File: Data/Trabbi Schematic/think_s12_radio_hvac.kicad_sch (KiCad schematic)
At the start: 20 parts, among them K1 Heated RW Relay R2, K2 Blower Relay R12, K3 Recirculation Relay R14, K4 Combustion Heater Relay R16, M1 Brake Vacuum Pump (E14), M2 Heater Blower Motor, M3 Recirculation Motor, SW1 Heater Switch, SW2 Recirculation Switch, SW3 Tailgate Release Switch, U1 Radio Unit, U2 Supplementary Heater (Webasto)

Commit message: Fix wire-to-pin connections: use exact calculated pin positions
Refactored gen_think_complete.py to compute exact pin schematic
coordinates instead of using approximate manual offsets. Added p()
method to Sheet class that transforms symbol-local pin positions to
schematic coordinates. All 232 wire calls across 13 sub-sheet
generators now use p() for pin endpoints, fixing misaligned
connections (previously off by 0.54-10+ units).

Co-Authored-By: Claude Opus 4.6 <noreply@anthropic.com>
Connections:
- net +12V_F1_HTDWS: now also K1.1 (86_COIL+)
- net +12V_F22_VACPUMP: now also M1.1 (+)
- net +12V_F33_WEBASTO: now also K4.1 (86_COIL+)
- net +12V_F3_HEATER: now also U2.1 (+12V)
- net +12V_F5_BLOWER: now also SW1.1 (IN), SW2.1 (A)
- net +12V_F7_RADIO: now also U1.1 (+12V_BAT)
- net +12V_F9_HORN_DOME: now also SW3.1 (A)
- net GND: now also HR1.2 (GND), LS1.2 (-), LS2.2 (-), M1.2 (-), M2.2 (M-), M3.2 (M-), SOL1.2 (-), U1.2 (GND), U1.5 (SPK_L-), U1.7 (SPK_R-), U2.2 (GND)
- net TAILGATE_RELEASE: now also SOL1.1 (+)
- net WEBASTO_CTRL: now also U2.5 (CTRL)
- net at HR1.1 (+12V): now also K1.3 (30_COM)
- net at M2.1 (M+): now also K2.3 (30_COM)
- net at SW2.2 (B): now also K3.1 (86_COIL+)
- net at LS1.1 (+): now also U1.4 (SPK_L+)
- net at U1.6 (SPK_R+): now also LS2.1 (+)
- net at M3.1 (M+): now also K3.3 (30_COM)
- net at K2.1 (86_COIL+): now also SW1.3 (SPD1)

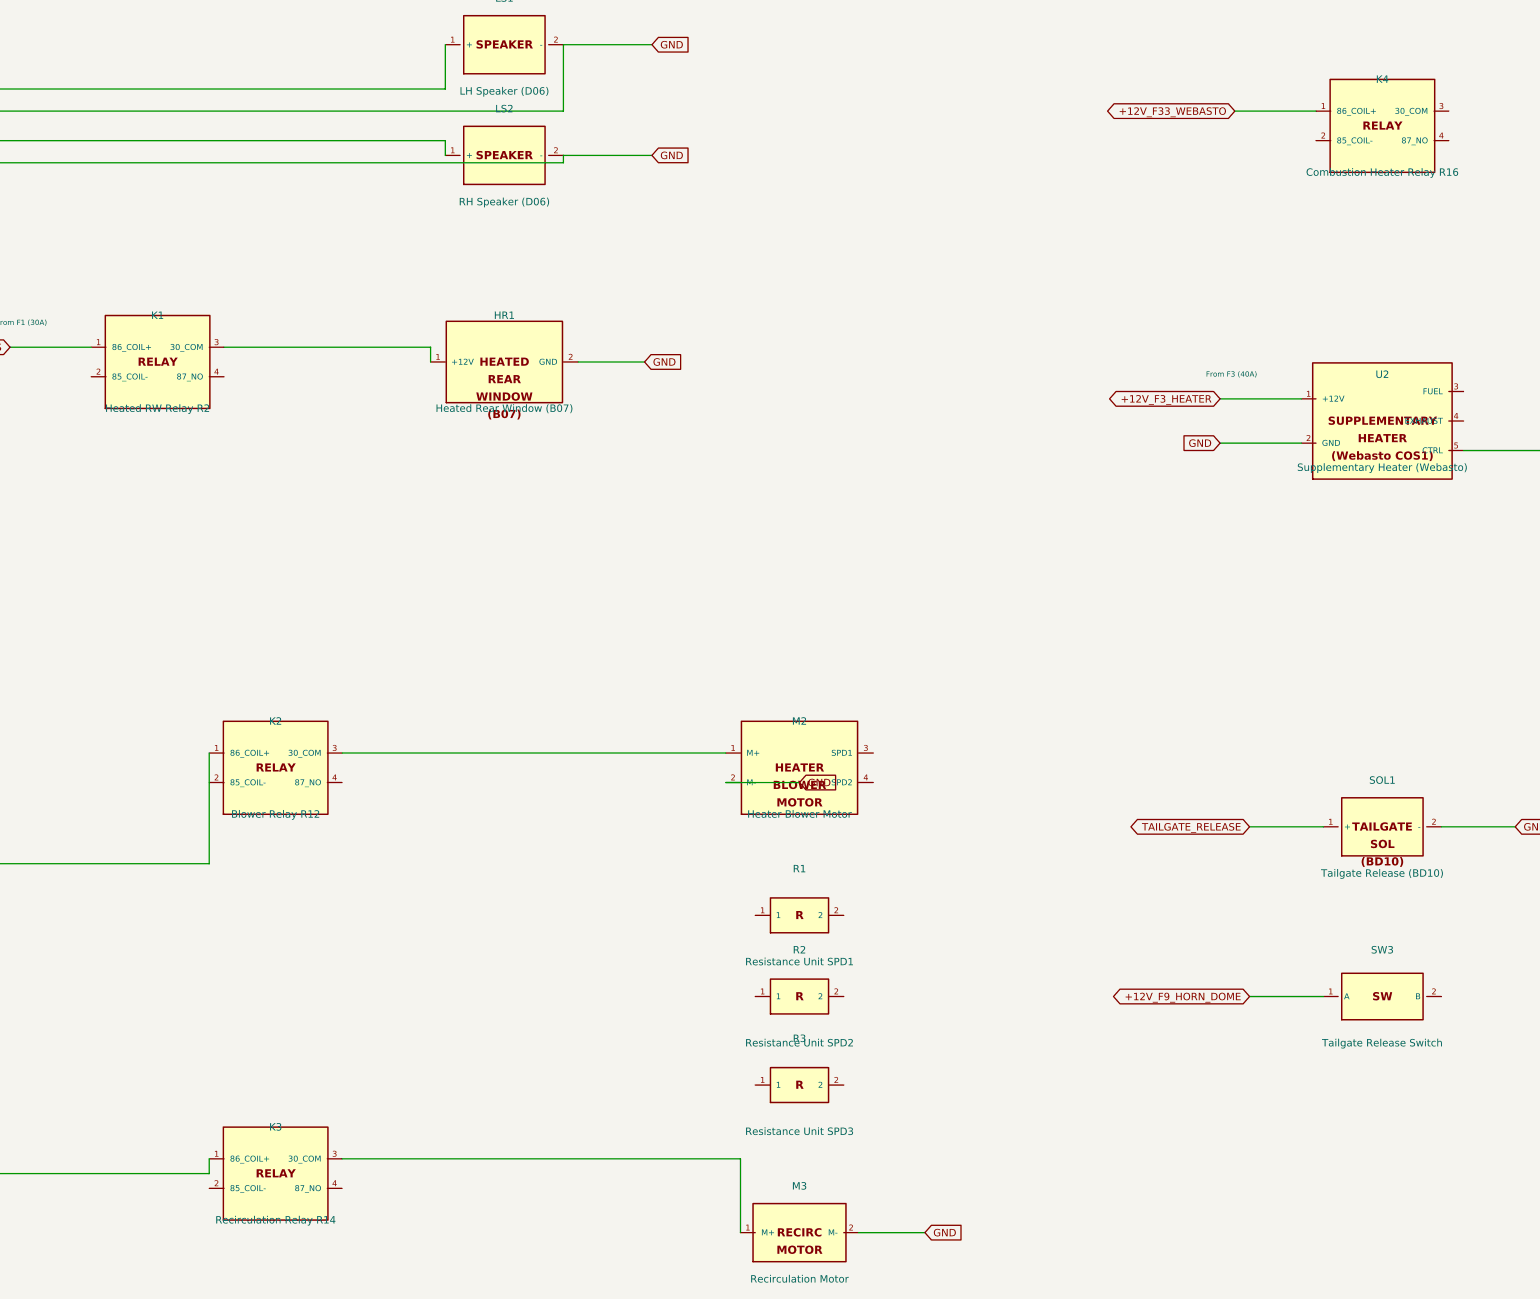
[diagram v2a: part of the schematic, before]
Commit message: Add relay coil/switch graphics, fix label positioning
- Draw coil (inductor arcs) and switch contacts (circles + arm)
  inside RELAY_SPST and RELAY_SPDT symbol bodies
- Add body_gfx parameter to defsym() for custom symbol graphics
- Helper functions: _gfx_polyline, _gfx_arc, _gfx_circle, _relay_gfx
- Fix label offsets: increase from 3-5mm to 10-12mm to avoid
  overlapping pin names (S01 ignition, S02 HV, S05 DCDC, S07 lights)
- Fix S09 turn signal rear labels: add wire stubs (were at 0 offset)
- All 14 schematics regenerated, parentheses balanced, grid OK

Co-Authored-By: Claude Opus 4.6 <noreply@anthropic.com>
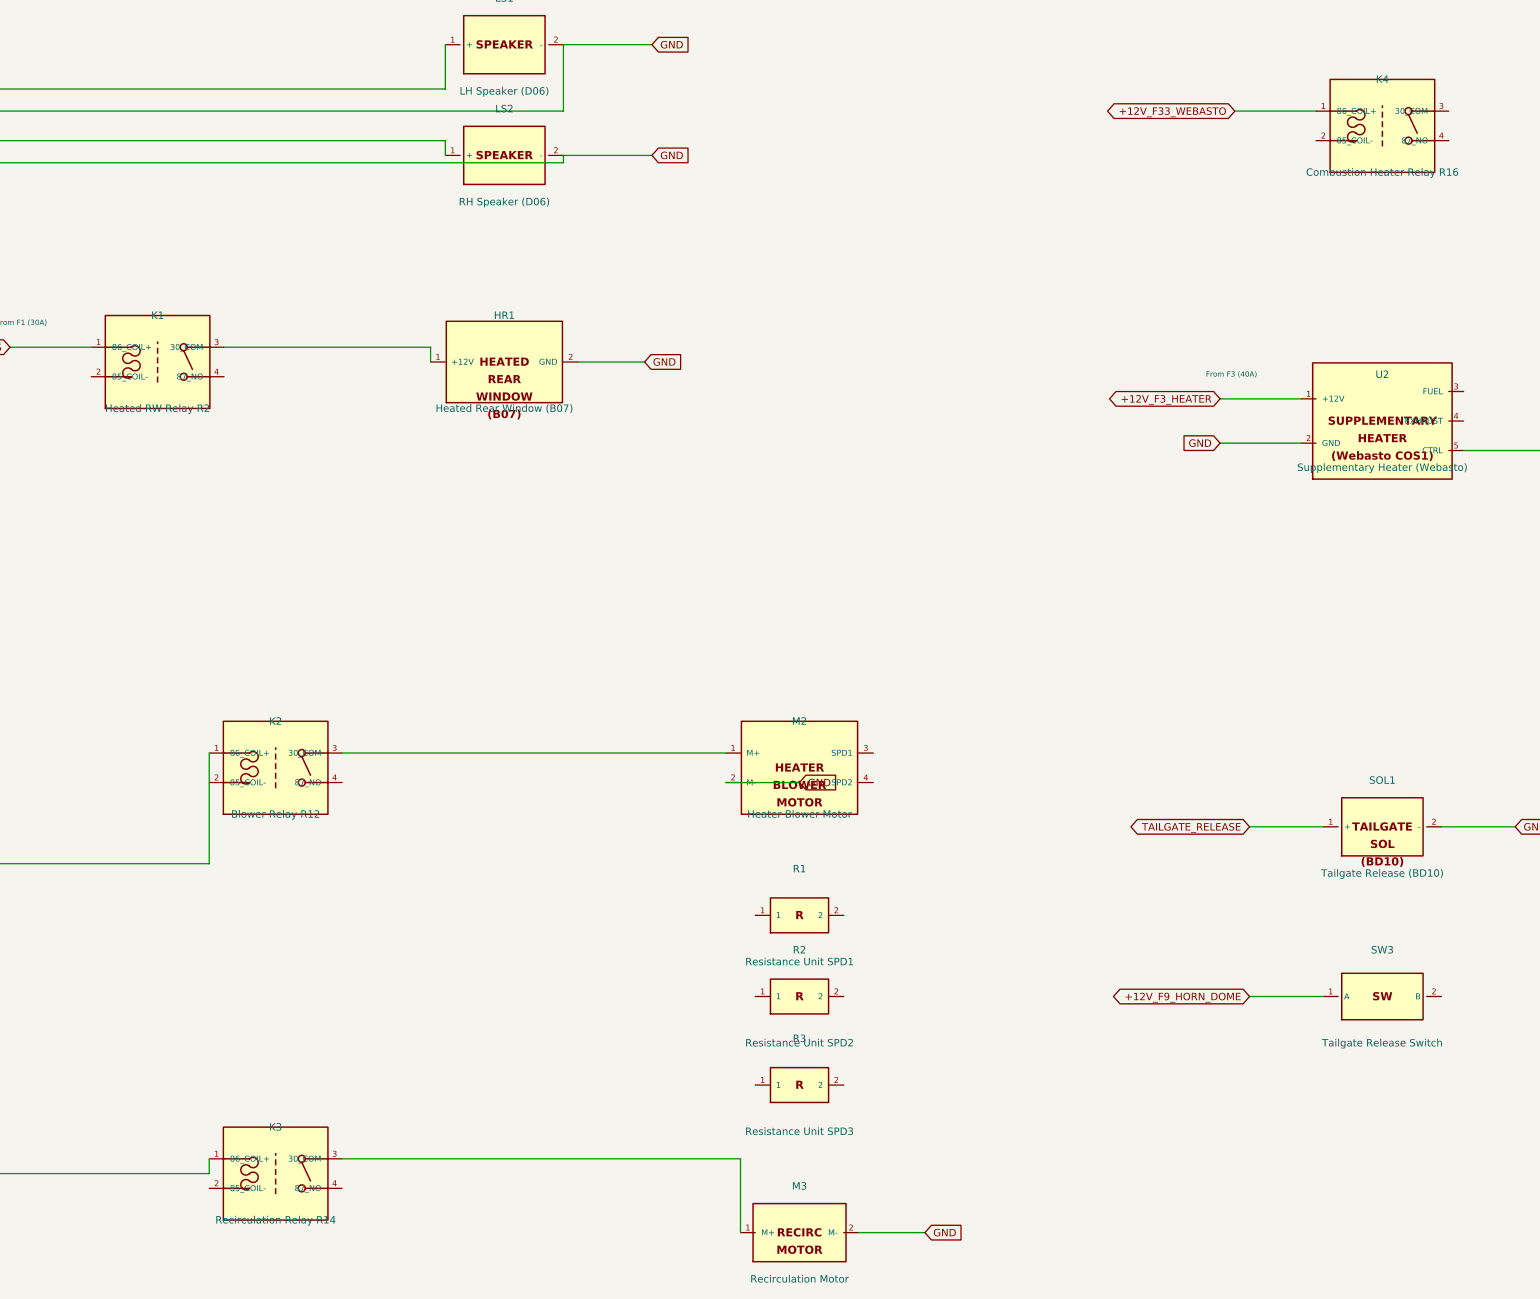
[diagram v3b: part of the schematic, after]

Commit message: Add cross-sheet reference annotations to global labels
- Track all global label positions per sheet during build
- After building all sheets, annotate each global label with
  "→S01,S03,..." text showing which other sheets share the net
- 60 cross-sheet nets identified and annotated
- Two-pass build: 1) build all sheets 2) add cross-refs + save
- Text placed near label in 0.8mm font, offset to avoid overlap

Co-Authored-By: Claude Opus 4.6 <noreply@anthropic.com>
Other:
- note added: "→S01"
- note added: "→S01,S02,S03,S04,S05,S06,S07,S08,S09,S10,S11,S13"
- note added: "→S01,S09,S10"
- note added: "→S10"
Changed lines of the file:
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@@
     (effects (font (size 1.000 1.000)))
+  )
+  (text "→S01" (at 47.800 46.950 0)
+    (effects (font (size 0.800 0.800)))
+  )
+  (text "→S01,S02,S03,S04,S05,S06,S07,S08,S09,S10,S11,S13" (at 47.800 52.030 0)
+    (effects (font (size 0.800 0.800)))
+  )
+  (text "→S01,S02,S03,S04,S05,S06,S07,S08,S09,S10,S11,S13" (at 229.060 38.060 0)
+    (effects (font (size 0.800 0.800)))
+  )
+  (text "→S01,S02,S03,S04,S05,S06,S07,S08,S09,S10,S11,S13" (at 229.060 57.110 0)
+    (effects (font (size 0.800 0.800)))
+  )
+  (text "→S01,S02,S03,S04,S05,S06,S07,S08,S09,S10,S11,S13" (at 227.790 92.670 0)
+    (effects (font (size 0.800 0.800)))
+  )
+  (text "→S01,S02,S03,S04,S05,S06,S07,S08,S09,S10,S11,S13" (at 109.680 121.880 0)
+    (effects (font (size 0.800 0.800)))
+  )
+  (text "→S01,S02,S03,S04,S05,S06,S07,S08,S09,S10,S11,S13" (at 251.920 165.060 0)
+    (effects (font (size 0.800 0.800)))
+  )
+  (text "→S01,S02,S03,S04,S05,S06,S07,S08,S09,S10,S11,S13" (at 276.050 242.530 0)
+    (effects (font (size 0.800 0.800)))
+  )
+  (text "→S01,S02,S03,S04,S05,S06,S07,S08,S09,S10,S11,S13" (at 318.310 106.640 0)
+    (effects (font (size 0.800 0.800)))
+  )
+  (text "→S01,S02,S03,S04,S05,S06,S07,S08,S09,S10,S11,S13" (at 377.650 172.680 0)
+    (effects (font (size 0.800 0.800)))
+  )
+  (text "→S01" (at 110.030 90.130 0)
+    (effects (font (size 0.800 0.800)))
+  )
+  (text "→S01" (at 50.340 121.880 0)
+    (effects (font (size 0.800 0.800)))
+  )
+  (text "→S01" (at 49.070 182.840 0)
+    (effects (font (size 0.800 0.800)))
+  )
+  (text "→S01" (at 49.070 232.370 0)
+    (effects (font (size 0.800 0.800)))
+  )
+  (text "→S01" (at 318.310 99.020 0)
+    (effects (font (size 0.800 0.800)))
+  )
+  (text "→S01" (at 320.850 49.490 0)
+    (effects (font (size 0.800 0.800)))
+  )
+  (text "→S10" (at 323.390 172.680 0)
+    (effects (font (size 0.800 0.800)))
+  )
+  (text "→S01,S09,S10" (at 323.390 201.890 0)
+    (effects (font (size 0.800 0.800)))
   )
   (symbol_instances)

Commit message: Fix label text justification for KiCad 9
Add (justify left) to all label and global_label effects.
KiCad 9 requires explicit text justification — without it,
label text is mispositioned relative to the label shape.

Co-Authored-By: Claude Opus 4.6 <noreply@anthropic.com>
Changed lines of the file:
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@@
   )
   (global_label "+12V_F7_RADIO" (shape bidirectional) (at 50.800 44.450 180)
-    (effects (font (size 1.27 1.27)))
+    (effects (font (size 1.27 1.27)) (justify left))
     (property "Intersheetrefs" "${INTERSHEET_REFS}" (at 50.800 44.450 0)
       (effects (font (size 1.27 1.27)) hide)
@@
   )
   (global_label "GND" (shape input) (at 50.800 49.530 180)
-    (effects (font (size 1.27 1.27)))
+    (effects (font (size 1.27 1.27)) (justify left))
     (property "Intersheetrefs" "${INTERSHEET_REFS}" (at 50.800 49.530 0)
       (effects (font (size 1.27 1.27)) hide)
@@
   )
   (global_label "GND" (shape input) (at 226.060 35.560 0)
-    (effects (font (size 1.27 1.27)))
+    (effects (font (size 1.27 1.27)) (justify left))
     (property "Intersheetrefs" "${INTERSHEET_REFS}" (at 226.060 35.560 0)
       (effects (font (size 1.27 1.27)) hide)
@@
   )
   (global_label "GND" (shape input) (at 226.060 54.610 0)
-    (effects (font (size 1.27 1.27)))
+    (effects (font (size 1.27 1.27)) (justify left))
     (property "Intersheetrefs" "${INTERSHEET_REFS}" (at 226.060 54.610 0)
       (effects (font (size 1.27 1.27)) hide)
@@
   )
   (label "ANT_SIGNAL" (at 58.420 17.780 0)
-    (effects (font (size 1.27 1.27)))
+    (effects (font (size 1.27 1.27)) (justify left))
   )
   (wire (pts (xy 64.770 54.610) (xy 64.770 20.320))
@@
   )
   (global_label "+12V_F1_HTDWS" (shape bidirectional) (at 113.030 87.630 180)
-    (effects (font (size 1.27 1.27)))
+    (effects (font (size 1.27 1.27)) (justify left))
     (property "Intersheetrefs" "${INTERSHEET_REFS}" (at 113.030 87.630 0)
       (effects (font (size 1.27 1.27)) hide)
@@
   )
   (global_label "GND" (shape input) (at 224.790 90.170 0)
-    (effects (font (size 1.27 1.27)))
+    (effects (font (size 1.27 1.27)) (justify left))
     (property "Intersheetrefs" "${INTERSHEET_REFS}" (at 224.790 90.170 0)
       (effects (font (size 1.27 1.27)) hide)
@@
   )
   (global_label "+12V_F22_VACPUMP" (shape bidirectional) (at 53.340 119.380 180)
-    (effects (font (size 1.27 1.27)))
+    (effects (font (size 1.27 1.27)) (justify left))
     (property "Intersheetrefs" "${INTERSHEET_REFS}" (at 53.340 119.380 0)
       (effects (font (size 1.27 1.27)) hide)
@@
   )
   (global_label "GND" (shape input) (at 106.680 119.380 0)
-    (effects (font (size 1.27 1.27)))
+    (effects (font (size 1.27 1.27)) (justify left))
     (property "Intersheetrefs" "${INTERSHEET_REFS}" (at 106.680 119.380 0)
       (effects (font (size 1.27 1.27)) hide)
@@
   )
   (global_label "+12V_F5_BLOWER" (shape bidirectional) (at 52.070 180.340 180)
-    (effects (font (size 1.27 1.27)))
+    (effects (font (size 1.27 1.27)) (justify left))
     (property "Intersheetrefs" "${INTERSHEET_REFS}" (at 52.070 180.340 0)
       (effects (font (size 1.27 1.27)) hide)
@@
   )
   (global_label "GND" (shape input) (at 248.920 162.560 0)
-    (effects (font (size 1.27 1.27)))
+    (effects (font (size 1.27 1.27)) (justify left))
     (property "Intersheetrefs" "${INTERSHEET_REFS}" (at 248.920 162.560 0)
       (effects (font (size 1.27 1.27)) hide)
@@
   )
   (global_label "+12V_F5_BLOWER" (shape bidirectional) (at 52.070 229.870 180)
-    (effects (font (size 1.27 1.27)))
+    (effects (font (size 1.27 1.27)) (justify left))
     (property "Intersheetrefs" "${INTERSHEET_REFS}" (at 52.070 229.870 0)
       (effects (font (size 1.27 1.27)) hide)
@@
   )
   (global_label "GND" (shape input) (at 273.050 240.030 0)
-    (effects (font (size 1.27 1.27)))
+    (effects (font (size 1.27 1.27)) (justify left))
     (property "Intersheetrefs" "${INTERSHEET_REFS}" (at 273.050 240.030 0)
       (effects (font (size 1.27 1.27)) hide)
@@
   )
   (global_label "+12V_F3_HEATER" (shape bidirectional) (at 321.310 96.520 180)
-    (effects (font (size 1.27 1.27)))
+    (effects (font (size 1.27 1.27)) (justify left))
     (property "Intersheetrefs" "${INTERSHEET_REFS}" (at 321.310 96.520 0)
       (effects (font (size 1.27 1.27)) hide)
@@
   )
   (global_label "GND" (shape input) (at 321.310 104.140 180)
-    (effects (font (size 1.27 1.27)))
+    (effects (font (size 1.27 1.27)) (justify left))
     (property "Intersheetrefs" "${INTERSHEET_REFS}" (at 321.310 104.140 0)
       (effects (font (size 1.27 1.27)) hide)
@@
   )
   (global_label "WEBASTO_CTRL" (shape bidirectional) (at 379.730 105.410 0)
-    (effects (font (size 1.27 1.27)))
+    (effects (font (size 1.27 1.27)) (justify left))
     (property "Intersheetrefs" "${INTERSHEET_REFS}" (at 379.730 105.410 0)
       (effects (font (size 1.27 1.27)) hide)
@@
   )
   (global_label "+12V_F33_WEBASTO" (shape bidirectional) (at 323.850 46.990 180)
-    (effects (font (size 1.27 1.27)))
+    (effects (font (size 1.27 1.27)) (justify left))
     (property "Intersheetrefs" "${INTERSHEET_REFS}" (at 323.850 46.990 0)
       (effects (font (size 1.27 1.27)) hide)
@@
   )
   (global_label "TAILGATE_RELEASE" (shape bidirectional) (at 326.390 170.180 180)
-    (effects (font (size 1.27 1.27)))
+    (effects (font (size 1.27 1.27)) (justify left))
     (property "Intersheetrefs" "${INTERSHEET_REFS}" (at 326.390 170.180 0)
       (effects (font (size 1.27 1.27)) hide)
@@
   )
   (global_label "GND" (shape input) (at 374.650 170.180 0)
-    (effects (font (size 1.27 1.27)))
+    (effects (font (size 1.27 1.27)) (justify left))
     (property "Intersheetrefs" "${INTERSHEET_REFS}" (at 374.650 170.180 0)
       (effects (font (size 1.27 1.27)) hide)
@@
   )
   (global_label "+12V_F9_HORN_DOME" (shape bidirectional) (at 326.390 199.390 180)
-    (effects (font (size 1.27 1.27)))
+    (effects (font (size 1.27 1.27)) (justify left))
     (property "Intersheetrefs" "${INTERSHEET_REFS}" (at 326.390 199.390 0)
       (effects (font (size 1.27 1.27)) hide)
